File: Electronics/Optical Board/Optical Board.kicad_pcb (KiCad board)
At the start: 2 copper layers, 30 x 30 mm, 6 parts, among them J2 OPTICAL

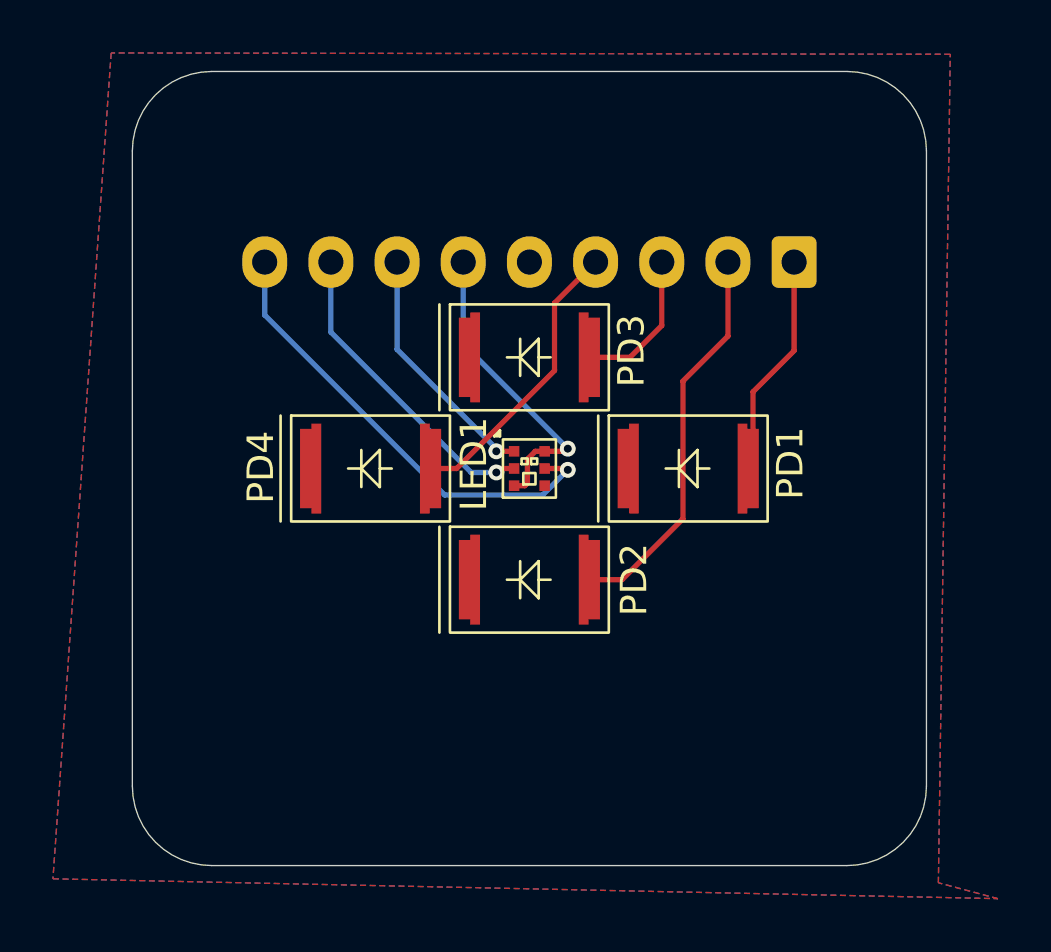
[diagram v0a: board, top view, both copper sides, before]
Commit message: Footprint changes
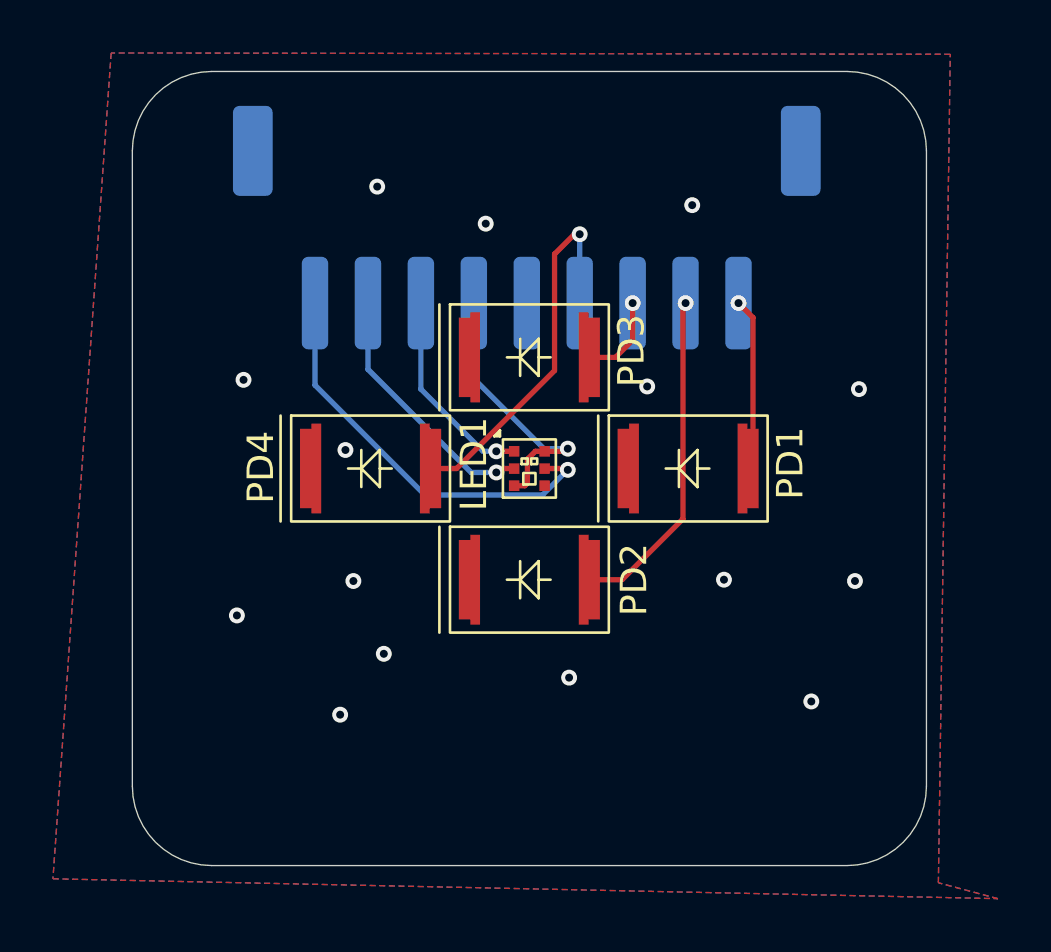
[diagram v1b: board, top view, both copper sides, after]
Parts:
- J2: footprint Connector_JST:JST_EH_S9B-EH_1x09_P2.50mm_Horizontal -> Connector_JST:JST_PH_S9B-PH-SM4-TB_1x09-1MP_P2.00mm_Horizontal
- moved J2 10.2 mm to (166.3, 64.3), turned to 0 degrees
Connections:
- J2 pad 1: /PD1 -> /LED3
- J2 pad 2: /PD2 -> /LED2
- J2 pad 3: /PD3 -> /LED1
- J2 pad 4: /PD4 -> +3V3
- J2 pad 6: +3V3 -> /PD4
- J2 pad 7: /LED1 -> /PD3
- J2 pad 8: /LED2 -> /PD2
- J2 pad 9: /LED3 -> /PD1
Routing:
- net /PD4: track 11.2 -> 14.7 mm, vias 0 -> 1
- net /LED2: track 12.7 -> 9.70 mm
- net /PD3: track 5.45 -> 3.12 mm, vias 0 -> 1
- net /LED3: track 17.9 -> 15.7 mm
- net /PD2: track 14.7 -> 12.5 mm, vias 0 -> 1
- net /PD1: track 8.44 -> 6.48 mm, vias 0 -> 1
- net /LED1: track 9.38 -> 7.75 mm
- net +3V3: track 11.8 -> 10.6 mm
- net /PD_K: vias 0 -> 15
